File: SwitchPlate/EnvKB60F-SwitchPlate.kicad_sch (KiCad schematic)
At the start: 157 parts, among them J1 TP3 Pad, J2 TP2 Pad, SW1 EVQ-P7A01P, U1 Pico

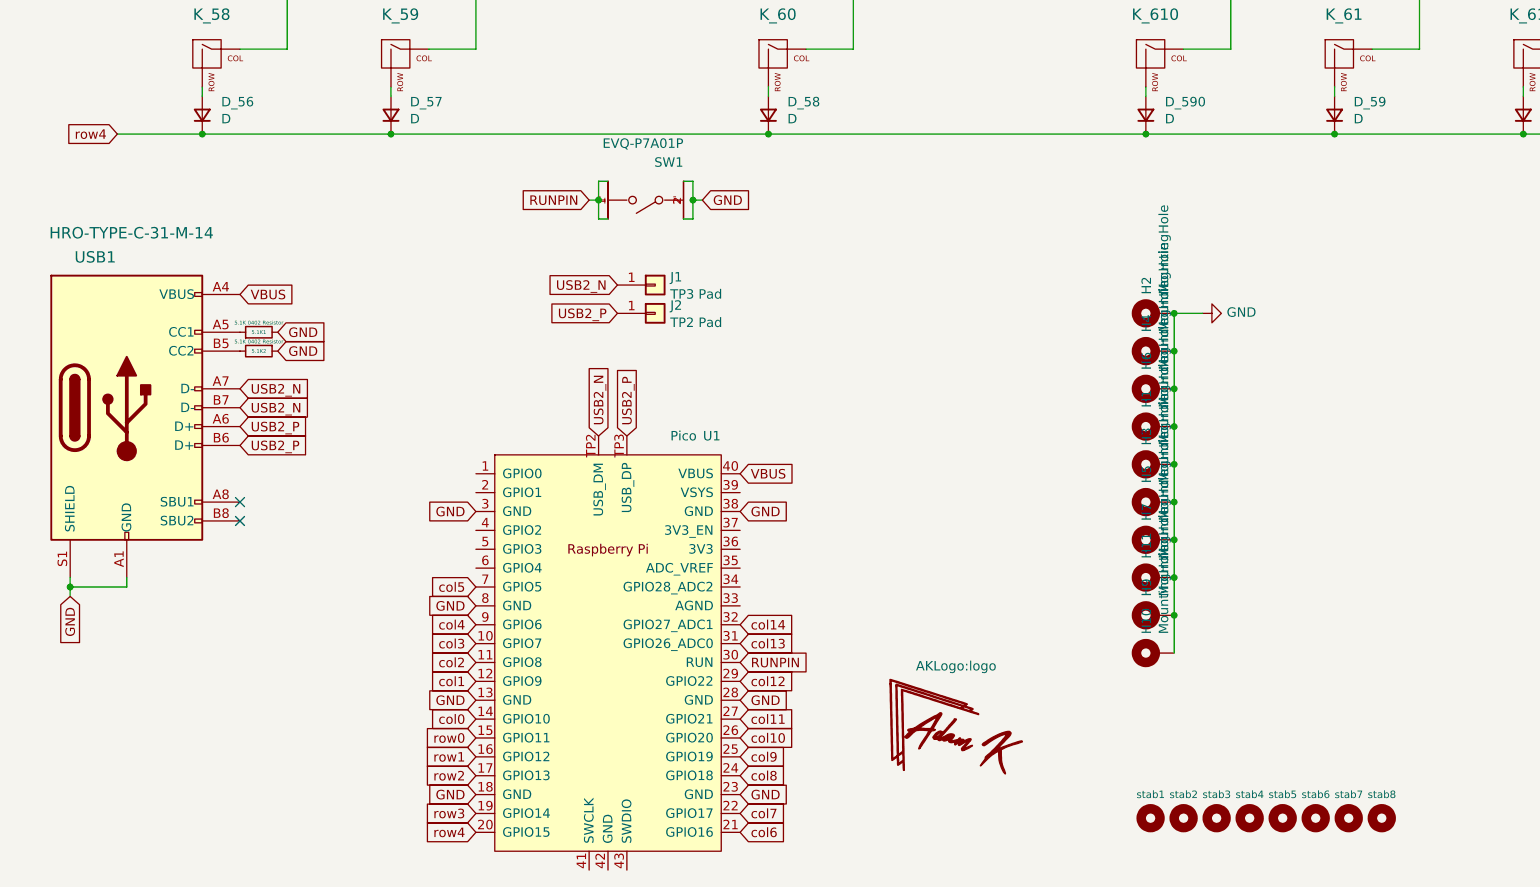
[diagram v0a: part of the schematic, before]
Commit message: updated backplate
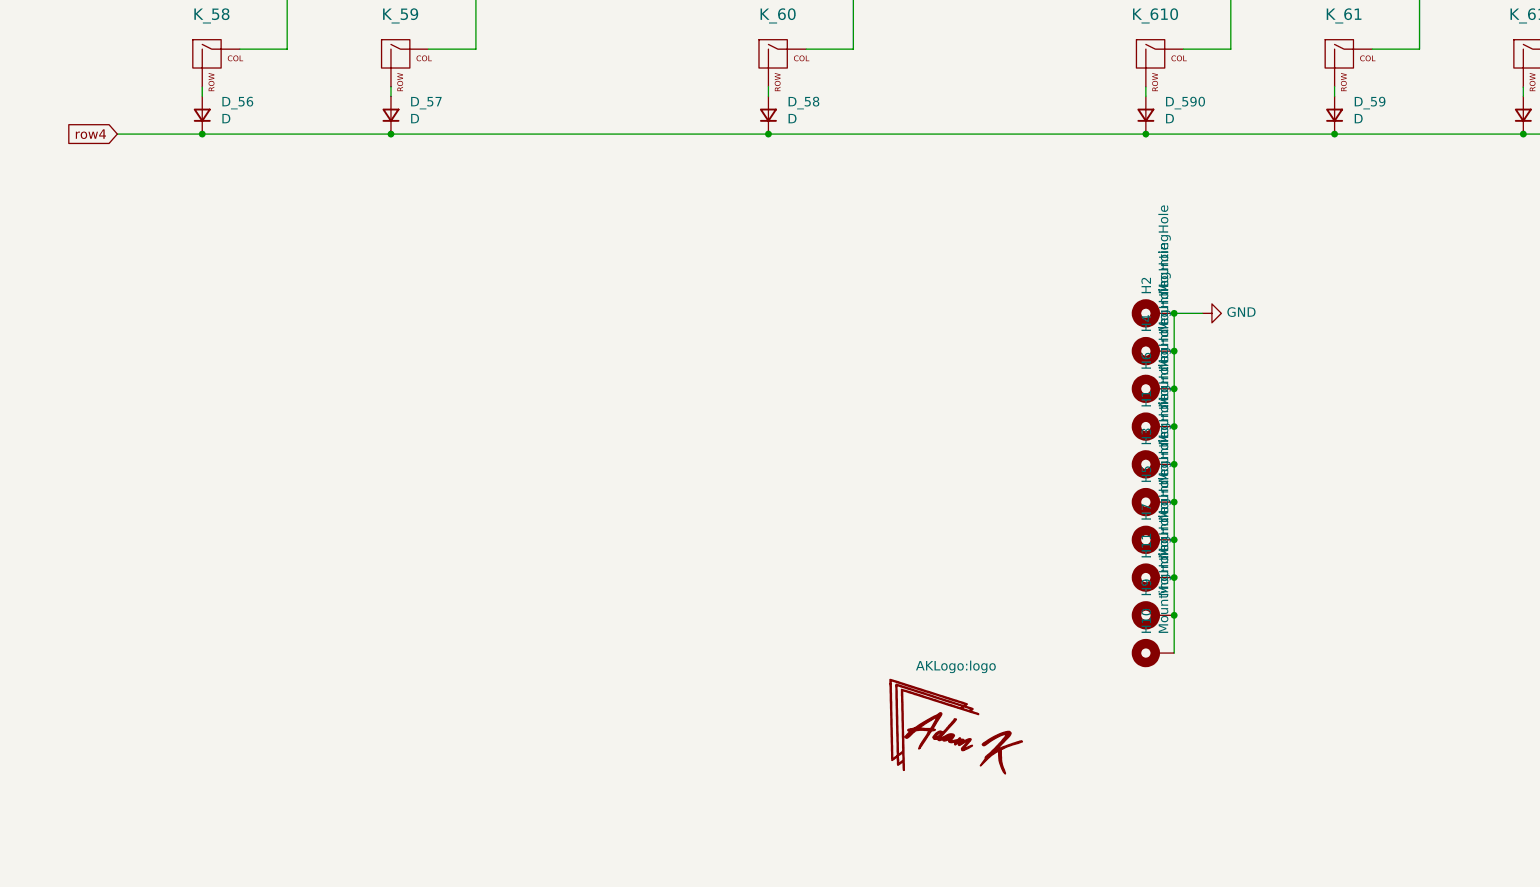
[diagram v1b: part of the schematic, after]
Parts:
- removed 5.1K1, 5.1K2: 5.1K 0402 Resistor, Resistor_THT:R_Axial_DIN0207_L6.3mm_D2.5mm_P10.16mm_Horizontal, symbol Device:R_Small
- removed J1: TP3 Pad, TestPoint:TestPoint_Pad_1.0x1.0mm, symbol Connector_Generic:Conn_01x01
- removed J2: TP2 Pad, TestPoint:TestPoint_Pad_1.0x1.0mm, symbol Connector_Generic:Conn_01x01
- removed SW1: EVQ-P7A01P, PanasonicEVQ-P7A01P:Panasonic-EVQ-P7A01P-0-0-MFG, symbol eec:EVQ-P7A01P
- removed U1: Pico, MCU_RaspberryPi_and_Boards:RPi_Pico_SMD_TH, symbol MCU_RaspberryPi_and_Boards:Pico
- removed USB1: HRO-TYPE-C-31-M-14, josh-connectors:USB_C_TYPE-C-31-M-14, symbol josh-connector:USB_C_U262-161N-4BVC11
- removed stab1, stab2, stab3, stab4, stab5, stab6, stab7, stab8: MX Stabilizer, Mounting_Keyboard_Stabilizer:Stabilizer_Cherry_MX_2u, symbol Mechanical:MountingHole
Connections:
- no-connect marks 2 -> 0
